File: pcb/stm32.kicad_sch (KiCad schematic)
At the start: 11 parts, among them U3 STM32F411RETx, Y2 12MHz

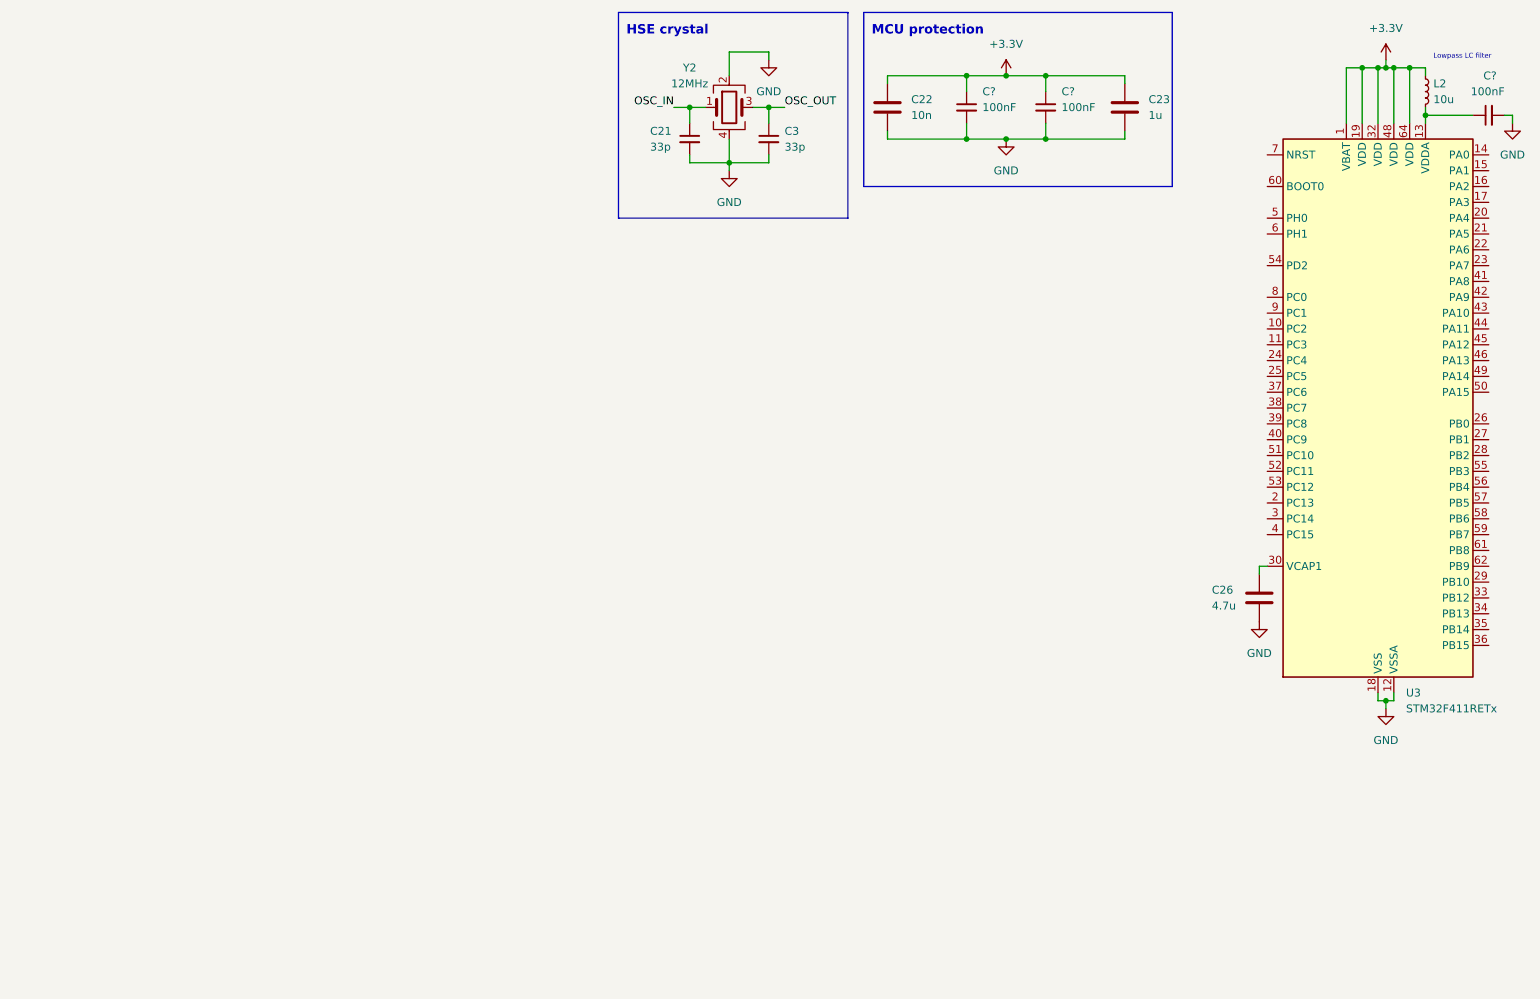
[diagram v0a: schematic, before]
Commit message: Finished off schematic
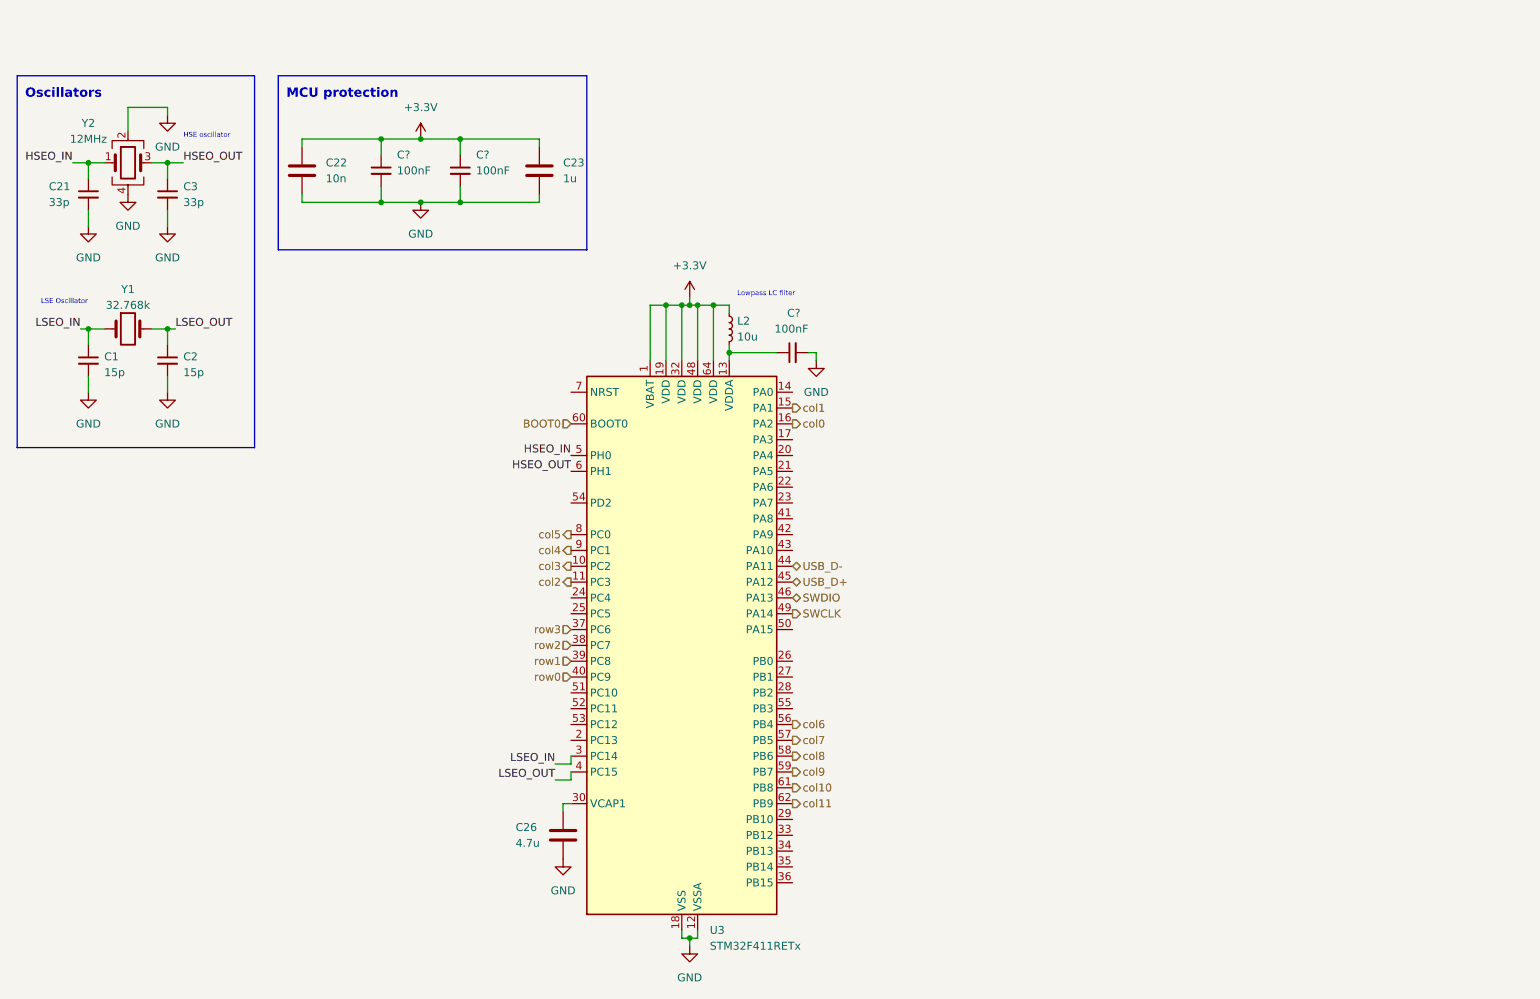
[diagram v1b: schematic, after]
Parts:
- added C1, C2: 15p, Capacitor_SMD:C_0805_2012Metric, symbol Device:C_Small
- added Y1: 32.768k, Crystal:Crystal_SMD_3215-2Pin_3.2x1.5mm, symbol Device:Crystal
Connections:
- net OSC_IN is gone; now on net HSEO_IN: C21.1, Y2.1
- net OSC_OUT is gone; now on net HSEO_OUT: C3.1, Y2.3
- net GND: now also C1.2, C2.2
- net col3: now reaches U3.10 (PC2)
- net col2: now reaches U3.11 (PC3)
- net col1: now reaches U3.15 (PA1)
- net col0: now reaches U3.16 (PA2)
- net LSEO_IN: now reaches U3.3 (PC14)
- net LSEO_IN: now also C1.1, Y1.1
- net row3: now reaches U3.37 (PC6)
- net row2: now reaches U3.38 (PC7)
- net row1: now reaches U3.39 (PC8)
- net LSEO_OUT: now reaches U3.4 (PC15)
- net LSEO_OUT: now also C2.1, Y1.2
- net row0: now reaches U3.40 (PC9)
- net USB_D-: now reaches U3.44 (PA11)
- net USB_D+: now reaches U3.45 (PA12)
- net SWDIO: now reaches U3.46 (PA13)
- net SWCLK: now reaches U3.49 (PA14)
- net HSEO_IN: now reaches U3.5 (PH0)
- net col6: now reaches U3.56 (PB4)
- net col7: now reaches U3.57 (PB5)
- net col8: now reaches U3.58 (PB6)
- net col9: now reaches U3.59 (PB7)
- net HSEO_OUT: now reaches U3.6 (PH1)
- net BOOT0: now reaches U3.60 (BOOT0)
- net col10: now reaches U3.61 (PB8)
- net col11: now reaches U3.62 (PB9)
- net col5: now reaches U3.8 (PC0)
- net col4: now reaches U3.9 (PC1)
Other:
- note added: "HSE oscillator"
- note added: "LSE Oscillator"
- note added: "Oscillators"
- note removed: "HSE crystal"
- moved on the sheet: C22, C23, C26, C?, L2, U3

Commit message: Started routing
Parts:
- C21, C3: LCSC (none) -> C157687
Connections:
- net col0: now also U3.50 (PA15); no longer U3.16 (PA2)
- net col1: now also U3.51 (PC10); no longer U3.15 (PA1)
- net col10: now also U3.42 (PA9); no longer U3.61 (PB8)
- net col11: now also U3.43 (PA10); no longer U3.62 (PB9)
- net col2: now also U3.52 (PC11); no longer U3.11 (PC3)
- net col3: now also U3.53 (PC12); no longer U3.10 (PC2)
- net col4: now also U3.54 (PD2); no longer U3.9 (PC1)
- net col5: now also U3.55 (PB3); no longer U3.8 (PC0)
- net col6: now also U3.38 (PC7); no longer U3.56 (PB4)
- net col7: now also U3.39 (PC8); no longer U3.57 (PB5)
- net col8: now also U3.40 (PC9); no longer U3.58 (PB6)
- net col9: now also U3.41 (PA8); no longer U3.59 (PB7)
- net row0: now also U3.61 (PB8); no longer U3.40 (PC9)
- net row1: now also U3.62 (PB9); no longer U3.39 (PC8)
- net row2: now also U3.29 (PB10); no longer U3.38 (PC7)
- net row3: now also U3.28 (PB2); no longer U3.37 (PC6)
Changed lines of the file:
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@@
-    (stroke (width 0) (type default))
-  )
-  (wire (pts (xy 114.3 135.89) (xy 114.3 134.62))
     (stroke (width 0) (type default))
   )
@@
     (stroke (width 0) (type default))
   )
-  (wire (pts (xy 111.76 135.89) (xy 114.3 135.89))
-    (stroke (width 0) (type default))
-  )
   (wire (pts (xy 132.08 62.23) (xy 129.54 62.23))
     (stroke (width 0) (type default))
@@
     (stroke (width 0) (type default))
   )
-  (wire (pts (xy 111.76 138.43) (xy 114.3 138.43))
-    (stroke (width 0) (type default))
-  )
   (wire (pts (xy 153.67 69.85) (xy 153.67 71.12))
     (stroke (width 0) (type default))
@@
   )
   (wire (pts (xy 49.53 66.04) (xy 49.53 68.58))
-    (stroke (width 0) (type default))
-  )
-  (wire (pts (xy 114.3 138.43) (xy 114.3 137.16))
     (stroke (width 0) (type default))
   )
@@
     (effects (font (size 1.27 1.27)) (justify left bottom))
   )
-  (label "LSEO_OUT" (at 111.76 138.43 180) (fields_autoplaced)
+  (label "LSEO_OUT" (at 114.3 137.16 180) (fields_autoplaced)
     (effects (font (size 1.27 1.27)) (justify right bottom))
   )
@@
     (effects (font (size 1.27 1.27)) (justify left bottom))
   )
-  (label "LSEO_IN" (at 111.76 135.89 180) (fields_autoplaced)
-    (effects (font (size 1.27 1.27)) (justify right bottom))
-  )
-  (hierarchical_label "col8" (shape output) (at 149.86 134.62 0) (fields_autoplaced)
-    (effects (font (size 1.27 1.27)) (justify left))
-  )
-  (hierarchical_label "col1" (shape output) (at 149.86 78.74 0) (fields_autoplaced)
-    (effects (font (size 1.27 1.27)) (justify left))
+  (label "LSEO_IN" (at 114.3 134.62 180) (fields_autoplaced)
+    (effects (font (size 1.27 1.27)) (justify right bottom))
+  )
+  (hierarchical_label "col8" (shape output) (at 114.3 121.92 180) (fields_autoplaced)
+    (effects (font (size 1.27 1.27)) (justify right))
+  )
+  (hierarchical_label "col1" (shape output) (at 114.3 124.46 180) (fields_autoplaced)
+    (effects (font (size 1.27 1.27)) (justify right))
   )
   (hierarchical_label "SWCLK" (shape output) (at 149.86 111.76 0) (fields_autoplaced)
     (effects (font (size 1.27 1.27)) (justify left))
   )
-  (hierarchical_label "row2" (shape input) (at 114.3 116.84 180) (fields_autoplaced)
-    (effects (font (size 1.27 1.27)) (justify right))
+  (hierarchical_label "row2" (shape input) (at 149.86 144.78 0) (fields_autoplaced)
+    (effects (font (size 1.27 1.27)) (justify left))
   )
   (hierarchical_label "SWDIO" (shape bidirectional) (at 149.86 109.22 0) (fields_autoplaced)
     (effects (font (size 1.27 1.27)) (justify left))
   )
-  (hierarchical_label "col4" (shape output) (at 114.3 101.6 180) (fields_autoplaced)
-    (effects (font (size 1.27 1.27)) (justify right))
-  )
-  (hierarchical_label "col11" (shape output) (at 149.86 142.24 0) (fields_autoplaced)
-    (effects (font (size 1.27 1.27)) (justify left))
-  )
-  (hierarchical_label "col3" (shape output) (at 114.3 104.14 180) (fields_autoplaced)
-    (effects (font (size 1.27 1.27)) (justify right))
-  )
-  (hierarchical_label "col10" (shape output) (at 149.86 139.7 0) (fields_autoplaced)
-    (effects (font (size 1.27 1.27)) (justify left))
-  )
-  (hierarchical_label "col7" (shape output) (at 149.86 132.08 0) (fields_autoplaced)
-    (effects (font (size 1.27 1.27)) (justify left))
-  )
-  (hierarchical_label "col6" (shape output) (at 149.86 129.54 0) (fields_autoplaced)
-    (effects (font (size 1.27 1.27)) (justify left))
-  )
-  (hierarchical_label "row3" (shape input) (at 114.3 114.3 180) (fields_autoplaced)
-    (effects (font (size 1.27 1.27)) (justify right))
+  (hierarchical_label "col4" (shape output) (at 114.3 93.98 180) (fields_autoplaced)
+    (effects (font (size 1.27 1.27)) (justify right))
+  )
+  (hierarchical_label "col11" (shape output) (at 149.86 101.6 0) (fields_autoplaced)
+    (effects (font (size 1.27 1.27)) (justify left))
+  )
+  (hierarchical_label "col3" (shape output) (at 114.3 129.54 180) (fields_autoplaced)
+    (effects (font (size 1.27 1.27)) (justify right))
+  )
+  (hierarchical_label "col10" (shape output) (at 149.86 99.06 0) (fields_autoplaced)
+    (effects (font (size 1.27 1.27)) (justify left))
+  )
+  (hierarchical_label "col7" (shape output) (at 114.3 119.38 180) (fields_autoplaced)
+    (effects (font (size 1.27 1.27)) (justify right))
+  )
+  (hierarchical_label "col6" (shape output) (at 114.3 116.84 180) (fields_autoplaced)
+    (effects (font (size 1.27 1.27)) (justify right))
+  )
+  (hierarchical_label "row3" (shape input) (at 149.86 124.46 0) (fields_autoplaced)
+    (effects (font (size 1.27 1.27)) (justify left))
   )
   (hierarchical_label "USB_D+" (shape bidirectional) (at 149.86 106.68 0) (fields_autoplaced)
@@
     (effects (font (size 1.27 1.27)) (justify left))
   )
-  (hierarchical_label "col5" (shape output) (at 114.3 99.06 180) (fields_autoplaced)
-    (effects (font (size 1.27 1.27)) (justify right))
-  )
-  (hierarchical_label "col9" (shape output) (at 149.86 137.16 0) (fields_autoplaced)
-    (effects (font (size 1.27 1.27)) (justify left))
-  )
-  (hierarchical_label "col2" (shape output) (at 114.3 106.68 180) (fields_autoplaced)
-    (effects (font (size 1.27 1.27)) (justify right))
-  )
-  (hierarchical_label "col0" (shape output) (at 149.86 81.28 0) (fields_autoplaced)
+  (hierarchical_label "col5" (shape output) (at 149.86 127 0) (fields_autoplaced)
+    (effects (font (size 1.27 1.27)) (justify left))
+  )
+  (hierarchical_label "col9" (shape output) (at 149.86 96.52 0) (fields_autoplaced)
+    (effects (font (size 1.27 1.27)) (justify left))
+  )
+  (hierarchical_label "col2" (shape output) (at 114.3 127 180) (fields_autoplaced)
+    (effects (font (size 1.27 1.27)) (justify right))
+  )
+  (hierarchical_label "col0" (shape output) (at 149.86 114.3 0) (fields_autoplaced)
     (effects (font (size 1.27 1.27)) (justify left))
   )
@@
     (effects (font (size 1.27 1.27)) (justify right))
   )
-  (hierarchical_label "row1" (shape input) (at 114.3 119.38 180) (fields_autoplaced)
-    (effects (font (size 1.27 1.27)) (justify right))
-  )
-  (hierarchical_label "row0" (shape input) (at 114.3 121.92 180) (fields_autoplaced)
-    (effects (font (size 1.27 1.27)) (justify right))
+  (hierarchical_label "row1" (shape input) (at 149.86 142.24 0) (fields_autoplaced)
+    (effects (font (size 1.27 1.27)) (justify left))
+  )
+  (hierarchical_label "row0" (shape input) (at 149.86 139.7 0) (fields_autoplaced)
+    (effects (font (size 1.27 1.27)) (justify left))
   )
   (symbol (lib_id "power:GND") (at 49.53 76.2 0) (unit 1)
@@
     )
     (property "Datasheet" "https://jlcpcb.com/partdetail/169035-0805CG330J500NT/C157687" (at 49.53 44.45 0)
+      (effects (font (size 1.27 1.27)) hide)
+    )
+    (property "LCSC" "C157687" (at 49.53 44.45 0)
       (effects (font (size 1.27 1.27)) hide)
     )
@@
       (effects (font (size 1.27 1.27)) hide)
     )
+    (property "LCSC" "C157687" (at 36.83 44.45 0)
+      (effects (font (size 1.27 1.27)) hide)
+    )

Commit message: Finished routing, ready for checks
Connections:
- net NRST: now reaches U3.7 (NRST)
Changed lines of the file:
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@@
     (effects (font (size 1.27 1.27)) (justify left))
+  )
+  (hierarchical_label "NRST" (shape input) (at 114.3 76.2 180) (fields_autoplaced)
+    (effects (font (size 1.27 1.27)) (justify right))
   )
   (hierarchical_label "col5" (shape output) (at 149.86 127 0) (fields_autoplaced)
